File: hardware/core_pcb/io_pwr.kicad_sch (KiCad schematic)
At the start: 72 parts, among them J13 FIELD A 24V, J14 FIELD B 24V, J15 PUMP POWER, J16 PUMP SIGNALS, J17 RELAY COILS, J18 USB-C, Q1 2N7002, Q2 BC817, Q3 BC807, Q4 2N7002, Q5 BC817, Q6 BC807, U17 L78L05, U18 ISO7741, U19 74LVC1G08, U20 74LVC1G08, U21 IPS7091S, U22 74LVC1G14, U23 74LVC1G14, U24 LMV331, U25 CPC1017N, U26 CPC1017N, U27 USBLC6-2SC6

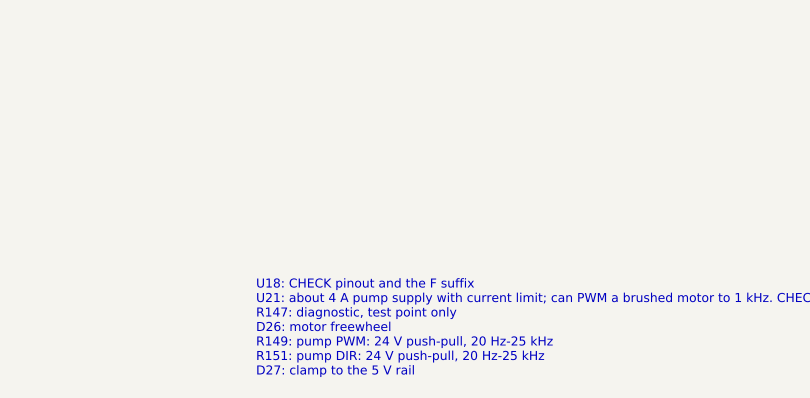
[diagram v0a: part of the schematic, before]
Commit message: CORE PCB: I/O chip pinouts checked against datasheets; gate latch, ODIS polarity
Pin tables of AD4112, ADS124S08, ISO2H823V2.5, ISO1I813T, ISO808A-1, ISO7741 and
ISOW7741 compared with the datasheets: all match. Fixes from the check: ISO2H823 /ODIS
is active low (takes GATE directly); OLADJ fitted 12.1k; CLKADJ 10k 0.1 %; ROSC 22.1k;
ISOW7741 EN/FLT pulled to 3.3 V; MAX6369 WDO only pulses, so a 74LVC1G175 latches a
trip until GATE_EN is re-armed. hardware/datasheets/IO_CHIPS_DATASHEET_CHECK.md holds the
extracts and the AD4112 register facts for the driver.

Co-Authored-By: Claude Opus 5.5 <noreply@anthropic.com>
Claude-Session: https://claude.ai/code/session_014onnq3eRiDkqdAB6fKiRDW
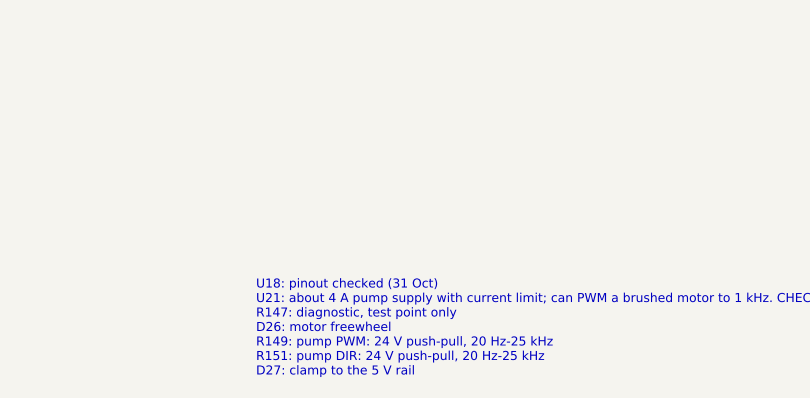
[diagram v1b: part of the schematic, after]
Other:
- note added: "U18: pinout checked (31 Oct) U21: about 4 A pump supply with current limit; can PWM a brushed motor to 1 kHz. CHECK rating once the 107Z current is known R147: diagnostic, test point only D26: motor freewheel R149: pump PWM: 24 V push-pull, 20 Hz-25 kHz R151: pump DIR: 24 V push-pull, 20 Hz-25 kHz D27: clamp to the 5 V rail"
- note removed: "U18: CHECK pinout and the F suffix U21: about 4 A pump supply with current limit; can PWM a brushed motor to 1 kHz. CHECK rating once the 107Z current is known R147: diagnostic, test point only D26: motor freewheel R149: pump PWM: 24 V push-pull, 20 Hz-25 kHz R151: pump DIR: 24 V push-pull, 20 Hz-25 kHz D27: clamp to the 5 V rail"
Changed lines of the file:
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@@
     (effects (font (size 1.0 1.0)) (justify left top))
   )
-  (text "\nU18: CHECK pinout and the F suffix\nU21: about 4 A pump supply with current limit; can PWM a brushed motor to 1 kHz. CHECK rating once the 107Z current is known\nR147: diagnostic, test point only\nD26: motor freewheel\nR149: pump PWM: 24 V push-pull, 20 Hz-25 kHz\nR151: pump DIR: 24 V push-pull, 20 Hz-25 kHz\nD27: clamp to the 5 V rail"
+  (text "\nU18: pinout checked (31 Oct)\nU21: about 4 A pump supply with current limit; can PWM a brushed motor to 1 kHz. CHECK rating once the 107Z current is known\nR147: diagnostic, test point only\nD26: motor freewheel\nR149: pump PWM: 24 V push-pull, 20 Hz-25 kHz\nR151: pump DIR: 24 V push-pull, 20 Hz-25 kHz\nD27: clamp to the 5 V rail"
     (at 203.2 347.98 0)
     (effects (font (size 1.0 1.0)) (justify left top))

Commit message: CORE PCB + breakout: make every user plug fit only its own header
Three pitch families (5.08 power/24 V outputs, 3.81 bank B, 3.5 sensors), one size per
header except the harmless temperature and 4-20 mA groups, and a coding key per header
(script-checked against every plug and shift). J13+J14 merged into one 4-way field plug;
pump power and signals on one 6-way plug (J16 gone); relays 3-way. Survival layer: 1k 1 W
pump outputs, per-channel relay PTCs + CPC1014N, 30 mA loop current limiters, TVS on the
5 V and 10 V sensor supplies. CORE_PCB.md section 15 has the mis-plug tables.

Co-Authored-By: Claude Opus 5.5 <noreply@anthropic.com>
Claude-Session: https://claude.ai/code/session_014onnq3eRiDkqdAB6fKiRDW
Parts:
- removed J14: FIELD B 24V, Connector_Phoenix_MSTB:PhoenixContact_MSTBVA_2,5_2-G-5,08_1x02_P5.08mm_Vertical, symbol Connector_Generic:Conn_01x02
- removed J16: PUMP SIGNALS, Connector_Phoenix_MC:PhoenixContact_MCV_1,5_4-G-3.81_1x04_P3.81mm_Vertical, symbol Connector_Generic:Conn_01x04
- added F22: 50mA, Fuse:Fuse_1206_3216Metric, symbol Device:Polyfuse
- F15: value 0.2A -> 50mA; MPN Bourns MF-NSMF020-2 -> Bourns MF-NSMF005-2
- J13: value FIELD A 24V -> FIELD 24V A+B; footprint Connector_Phoenix_MSTB:PhoenixContact_MSTBVA_2,5_2-G-5,08_1x02_P5.08mm_Vertical -> Connector_Phoenix_MSTB:PhoenixContact_MSTBVA_2,5_4-G-5,08_1x04_P5.08mm_Vertical; symbol Connector_Generic:Conn_01x02 -> Connector_Generic:Conn_01x04; MPN Phoenix MSTBVA 2,5/2-G-5,08 + plug (12 A) -> Phoenix MSTBVA 2,5/4-G-5,08 + coded, labelled plug; coding 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
- J15: value PUMP POWER -> PUMP; footprint Connector_Phoenix_MSTB:PhoenixContact_MSTBVA_2,5_2-G-5,08_1x02_P5.08mm_Vertical -> Connector_Phoenix_MSTB:PhoenixContact_MSTBVA_2,5_6-G-5,08_1x06_P5.08mm_Vertical; symbol Connector_Generic:Conn_01x02 -> Connector_Generic:Conn_01x06; MPN Phoenix MSTBVA 2,5/2-G-5,08 + plug -> Phoenix MSTBVA 2,5/6-G-5,08 + coded, labelled plug; coding 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
- J17: footprint Connector_Phoenix_MC:PhoenixContact_MCV_1,5_4-G-3.81_1x04_P3.81mm_Vertical -> Connector_Phoenix_MSTB:PhoenixContact_MSTBVA_2,5_3-G-5,08_1x03_P5.08mm_Vertical; symbol Connector_Generic:Conn_01x04 -> Connector_Generic:Conn_01x03; MPN Phoenix MCV 1,5/4-G-3,81 (or Degson / Dinkle equivalent) + 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 -> Phoenix MSTBVA 2,5/3-G-5,08 + coded, labelled plug; coding 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
- R149, R151: value 47R -> 1k 1W; footprint Resistor_SMD:R_0805_2012Metric -> Resistor_SMD:R_2512_6332Metric; MPN 47R -> anti-surge 2512, 1 W
- U25, U26: MPN IXYS CPC1017NTR -> IXYS CPC1014NTR
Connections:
- net +24V_FB: now also F22.1
- net FB_IN: now also J13.3 (Pin_3)
- net FIELD_0V: now also J13.4 (Pin_4), J15.6 (Pin_6), J17.3 (Pin_3); no longer J17.2 (Pin_2), J17.4 (Pin_4)
- net P_DIR_OUT: now also J15.4 (Pin_4)
- net P_PWM_OUT: now also J15.3 (Pin_3)
- net P_TACH_IN: now also J15.5 (Pin_5)
- net REL2_OUT: now also J17.2 (Pin_2); no longer J17.3 (Pin_3)
- net +24V_REL renamed +24V_REL1
- net +24V_REL1: no longer U26.3
- new net +24V_REL2: F22.2, U26.3
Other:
- note added: "Notes J13: one 4-way plug for both field supplies (12 A per contact): A = bank A, inputs, pump (about 10 A); B = bank B and relays (about 8 A). Link A and B in the plug for a single supply F12: bank A, inputs, ribbons F13: pump F14: bank B, relays D21: unidirectional TVS: surge clamp, and blows the fuse on reverse polarity U17: pump logic 5 V, field side U18: pinout checked (31 Oct)"
- note added: "U21: about 4 A pump supply with current limit; can PWM a brushed motor to 1 kHz. CHECK rating once the 107Z current is known R147: diagnostic, test point only D26: motor freewheel R149: pump PWM: 24 V push-pull, 20 Hz-25 kHz. 1k makes the output survive a short to 0 V or 24 V for ever (24 mA, 0.6 W). CHECK the 107Z input current (high level = 24 V - 1k x I) R151: pump DIR: 24 V push-pull, 20 Hz-2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"
- note added: "U24: CHECK pin order for the SOT-23-5 variant R156: hysteresis JP2: fit for an open-collector tacho J15: one plug for the whole pump: power, 0 V, PWM, DIR, tacho, signal 0 V (Thomas 107Z: signal ground must be field 0 V) F15: per-channel limit: a shorted coil wire trips only its own PTC U25: 60 V, 400 mA PhotoMOS: rides out a short until its PTC trips. CHECK with a 10 s short test R163: 5 V -> 3.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"
- note removed: "Notes J13: bank A, inputs, pump: about 10 A J14: bank B and relays: about 8 A F12: bank A, inputs, ribbons F13: pump F14: bank B, relays D21: unidirectional TVS: surge clamp, and blows the fuse on reverse polarity U17: pump logic 5 V, field side"
- note removed: "R154: 1.5 V threshold U24: CHECK pin order for the SOT-23-5 variant R156: hysteresis JP2: fit for an open-collector tacho J16: Thomas 107Z: signal ground must be field 0 V U25: 60 V, 100 mA PhotoMOS R163: 5 V -> 3.4 V"
- note removed: "U18: pinout checked (31 Oct) U21: about 4 A pump supply with current limit; can PWM a brushed motor to 1 kHz. CHECK rating once the 107Z current is known R147: diagnostic, test point only D26: motor freewheel R149: pump PWM: 24 V push-pull, 20 Hz-25 kHz R151: pump DIR: 24 V push-pull, 20 Hz-25 kHz D27: clamp to the 5 V rail"
- moved on the sheet: C125, C126, C127, C128, C129, C130, C131, C132, C133, C134, C135, C201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

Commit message: CORE PCB: fit-optional 4 x 4-20 mA analog outputs (AD5755-1, all DNP)
AD5755-1 on the analog island with its own ISOW7741 (CS_AO on PD3) and an ITX2405SA for
the boost converters; keyed 8-way 3.5 mm J26 (keys 2, 6, script-checked). Pin numbers from
the datasheet Table 5. Layout block plan now 2.8 mm over in io_pwr: the board is full
single-sided, see thread for the module option.

Co-Authored-By: Claude Opus 5.5 <noreply@anthropic.com>
Claude-Session: https://claude.ai/code/session_014onnq3eRiDkqdAB6fKiRDW
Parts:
- removed R143: 10k, Resistor_SMD:R_0805_2012Metric, symbol Device:R
- added R164: 68k, Resistor_SMD:R_0603_1608Metric, symbol Device:R
- R145: value 100k -> 10k; footprint Resistor_SMD:R_0603_1608Metric -> Resistor_SMD:R_0805_2012Metric; MPN 100k -> 10k
- R147: value 10k -> 100k; MPN 10k -> 100k
- R148: footprint Resistor_SMD:R_0805_2012Metric -> Resistor_SMD:R_0603_1608Metric
- R149, R151: value 1k 1W -> 10k; footprint Resistor_SMD:R_2512_6332Metric -> Resistor_SMD:R_0805_2012Metric; MPN anti-surge 2512, 1 W -> 10k
- R150, R152: value 10k -> 1k 1W; footprint Resistor_SMD:R_0805_2012Metric -> Resistor_SMD:R_2512_6332Metric; MPN 10k -> anti-surge 2512, 1 W
- R153: footprint Resistor_SMD:R_0603_1608Metric -> Resistor_SMD:R_0805_2012Metric
- R154: value 4k3 -> 10k; MPN 4k3 -> 10k
- R155: value 10k -> 4k3; MPN 10k -> 4k3
- R156: value 1M -> 10k; MPN 1M -> 10k
- R157: value 4k7 -> 1M; MPN 4k7 -> 1M
- R158: value 330R -> 4k7; MPN 330R -> 4k7
- R160: value 5k1 -> 330R; MPN 5k1 -> 330R
- R162: value 33k -> 5k1; MPN 33k -> 5k1
- R163: value 68k -> 33k; MPN 68k -> 33k
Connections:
- net +24V_FA: now also R144.1, R149.1, R151.1; no longer R148.1, R150.1
- net +24V_FB: now also R145.1; no longer R144.1
- net +5V_P: now also R148.1, R154.1, R156.1, R158.1; no longer R147.1, R153.1, R155.1, R157.1
- net FA_LED_A: now also R144.2
- net FB_LED_A: now also R145.2; no longer R144.2
- net FIELD_0V: now also R155.2; no longer R154.2
- net GATE: now also R160.1; no longer R158.1
- net GND: now also R147.2, R162.2, R164.2; no longer R145.2, R160.2, R163.2
- net PUMP_EN: now also R146.1; no longer R145.1
- net PUMP_PWM: now also R147.1; no longer R146.1
- net P_DG: now also R148.2; no longer R147.2
- net P_DIR_B: now also R151.2; no longer R150.2
- net P_DIR_E: now also R152.1; no longer R151.1
- net P_DIR_OUT: now also R152.2; no longer R151.2
- net P_PWM_B: now also R149.2; no longer R148.2
- net P_PWM_E: now also R150.1; no longer R149.1
- net P_PWM_OUT: now also R150.2; no longer R149.2
- net P_TACH_C: now also R153.2, R157.2; no longer R152.2, R156.2
- net P_TACH_F: now also R156.2, R157.1; no longer R155.2, R156.1
- net P_TACH_IN: now also R153.1; no longer R152.1
- net P_TACH_PU: now also R158.2; no longer R157.2
- net P_TREF: now also R154.2, R155.1; no longer R153.2, R154.1
- net REL1_A: now also R159.2; no longer R158.2
- net REL2_A: now also R160.2; no longer R159.2
- net USB_CC1: now also R161.1; no longer R160.1
- net USB_CC2: now also R162.1; no longer R161.1
- net USB_VBUS_SNS: now also R163.2, R164.1; no longer R162.2, R163.1
- net VBUS_USB: now also R163.1; no longer R162.1
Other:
- note added: "U21: about 4 A pump supply with current limit; can PWM a brushed motor to 1 kHz. CHECK rating once the 107Z current is known R148: diagnostic, test point only D26: motor freewheel R150: pump PWM: 24 V push-pull, 20 Hz-25 kHz. 1k makes the output survive a short to 0 V or 24 V for ever (24 mA, 0.6 W). CHECK the 107Z input current (high level = 24 V - 1k x I) R152: pump DIR: 24 V push-pull, 20 Hz-2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"
- note added: "U24: CHECK pin order for the SOT-23-5 variant R157: hysteresis JP2: fit for an open-collector tacho J15: one plug for the whole pump: power, 0 V, PWM, DIR, tacho, signal 0 V (Thomas 107Z: signal ground must be field 0 V) F15: per-channel limit: a shorted coil wire trips only its own PTC U25: 60 V, 400 mA PhotoMOS: rides out a short until its PTC trips. CHECK with a 10 s short test R164: 5 V -> 3.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"
- note removed: "U21: about 4 A pump supply with current limit; can PWM a brushed motor to 1 kHz. CHECK rating once the 107Z current is known R147: diagnostic, test point only D26: motor freewheel R149: pump PWM: 24 V push-pull, 20 Hz-25 kHz. 1k makes the output survive a short to 0 V or 24 V for ever (24 mA, 0.6 W). CHECK the 107Z input current (high level = 24 V - 1k x I) R151: pump DIR: 24 V push-pull, 20 Hz-2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"
- note removed: "U24: CHECK pin order for the SOT-23-5 variant R156: hysteresis JP2: fit for an open-collector tacho J15: one plug for the whole pump: power, 0 V, PWM, DIR, tacho, signal 0 V (Thomas 107Z: signal ground must be field 0 V) F15: per-channel limit: a shorted coil wire trips only its own PTC U25: 60 V, 400 mA PhotoMOS: rides out a short until its PTC trips. CHECK with a 10 s short test R163: 5 V -> 3.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"
- moved on the sheet: R144, R145, R146, R147, R148, R149, R150, R151, R152, R153, R154, R155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

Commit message: CORE PCB: SPI expansion header J26 for plug-on modules; analog outputs move off the core
Gary: analog out as an add-on module. J26 10-way latched IDC: +24 V and +3.3 V behind PTCs,
SPI4 through 100R, MISO buffered by a 74LVC1G125 enabled by CS_EXP (PD3), EXP_INT on PD7.
The AD5755-1 block drafted in 04adb9f is removed from the core and will become the module.
Layout block plan fits again. CORE_PCB.md section 16.

Co-Authored-By: Claude Opus 5.5 <noreply@anthropic.com>
Claude-Session: https://claude.ai/code/session_014onnq3eRiDkqdAB6fKiRDW
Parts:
- removed C125: 330n 50V, Capacitor_SMD:C_0603_1608Metric, symbol Device:C
- removed C126: 1u, Capacitor_SMD:C_0603_1608Metric, symbol Device:C
- removed R144, R145: 10k, Resistor_SMD:R_0805_2012Metric, symbol Device:R
- removed R146, R147: 100k, Resistor_SMD:R_0603_1608Metric, symbol Device:R
- removed R148: 10k, Resistor_SMD:R_0603_1608Metric, symbol Device:R
- added C136: 1n, Capacitor_SMD:C_0603_1608Metric, symbol Device:C
- added C137: 100n, Capacitor_SMD:C_0603_1608Metric, symbol Device:C
- added R165: 330R, Resistor_SMD:R_0603_1608Metric, symbol Device:R
- added R166, R167: 5k1, Resistor_SMD:R_0603_1608Metric, symbol Device:R
- added R168: 33k, Resistor_SMD:R_0603_1608Metric, symbol Device:R
- added R169: 68k, Resistor_SMD:R_0603_1608Metric, symbol Device:R
- C127: value 100n -> 330n 50V; MPN 100n -> 330n 50V
- C128: value 100n -> 1u; MPN 100n -> 1u
- C131: value 100n 50V -> 100n; MPN 100n 50V -> 100n
- C133: value 100n -> 100n 50V; MPN 100n -> 100n 50V
- C134: value 1n -> 100n; MPN 1n -> 100n
- R150: value 1k 1W -> 10k; footprint Resistor_SMD:R_2512_6332Metric -> Resistor_SMD:R_0805_2012Metric; MPN anti-surge 2512, 1 W -> 10k
- R151: value 10k -> 100k; footprint Resistor_SMD:R_0805_2012Metric -> Resistor_SMD:R_0603_1608Metric; MPN 10k -> 100k
- R152: value 1k 1W -> 100k; footprint Resistor_SMD:R_2512_6332Metric -> Resistor_SMD:R_0603_1608Metric; MPN anti-surge 2512, 1 W -> 100k
- R153: footprint Resistor_SMD:R_0805_2012Metric -> Resistor_SMD:R_0603_1608Metric
- R154, R156: footprint Resistor_SMD:R_0603_1608Metric -> Resistor_SMD:R_0805_2012Metric
- R155: value 4k3 -> 1k 1W; footprint Resistor_SMD:R_0603_1608Metric -> Resistor_SMD:R_2512_6332Metric; MPN 4k3 -> anti-surge 2512, 1 W
- R157: value 1M -> 1k 1W; footprint Resistor_SMD:R_0603_1608Metric -> Resistor_SMD:R_2512_6332Metric; MPN 1M -> anti-surge 2512, 1 W
- R158: value 4k7 -> 10k; footprint Resistor_SMD:R_0603_1608Metric -> Resistor_SMD:R_0805_2012Metric; MPN 4k7 -> 10k
- R159: value 330R -> 10k; MPN 330R -> 10k
- R160: value 330R -> 4k3; MPN 330R -> 4k3
- R161: value 5k1 -> 10k; MPN 5k1 -> 10k
- R162: value 5k1 -> 1M; MPN 5k1 -> 1M
- R163: value 33k -> 4k7; MPN 33k -> 4k7
- R164: value 68k -> 330R; MPN 68k -> 330R
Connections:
- net +24V_FA: now also C127.1, R154.1, R156.1; no longer R151.1
- net +24V_FB: now also R150.1
- net +24V_FP: now also C133.1; no longer C131.1
- net +3V3: now also C130.1, C131.1; no longer C127.1, C128.1
- net +5V_P: now also C128.1, C134.1, R153.1, R159.1, R161.1, R163.1, C137.1; no longer C130.1, C133.1, R154.1, R156.1, R158.1
- net FA_LED_A: now also R149.2
- net FB_LED_A: now also R150.2
- net FIELD_0V: now also C127.2, C128.2, R160.2, C136.2, C137.2; no longer C130.2, C131.2, R155.2
- net GATE: now also R164.1, R165.1; no longer R159.1, R160.1
- net GND: now also C130.2, C131.2, R151.2, R152.2, R166.2, R167.2, R169.2; no longer C127.2, C128.2, R161.2, R162.2, R164.2
- net PUMP_EN: now also R151.1
- net PUMP_PWM: now also R152.1
- net P_DG: now also R153.2
- net P_DIR_B: now also R156.2; no longer R151.2
- net P_DIR_E: now also R157.1; no longer R152.1
- net P_DIR_OUT: now also R157.2; no longer R152.2
- net P_PWM_B: now also R154.2; no longer R149.2
- net P_PWM_E: now also R155.1; no longer R150.1
- net P_PWM_OUT: now also R155.2; no longer R150.2
- net P_TACH_C: now also R158.2, R162.2, C136.1; no longer C134.1, R153.2, R157.2
- net P_TACH_F: now also R161.2, R162.1; no longer R156.2, R157.1
- net P_TACH_IN: now also R158.1; no longer R153.1
- net P_TACH_PU: now also R163.2; no longer R158.2
- net P_TREF: now also R159.2, R160.1; no longer R154.2, R155.1
- net REL1_A: now also R164.2; no longer R159.2
- net REL2_A: now also R165.2; no longer R160.2
- net USB_CC1: now also R166.1; no longer R161.1
- net USB_CC2: now also R167.1; no longer R162.1
- net USB_VBUS_SNS: now also R168.2, R169.1; no longer R163.2, R164.1
- net VBUS_USB: now also R168.1; no longer R163.1
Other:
- note added: "U21: about 4 A pump supply with current limit; can PWM a brushed motor to 1 kHz. CHECK rating once the 107Z current is known R153: diagnostic, test point only D26: motor freewheel R155: pump PWM: 24 V push-pull, 20 Hz-25 kHz. 1k makes the output survive a short to 0 V or 24 V for ever (24 mA, 0.6 W). CHECK the 107Z input current (high level = 24 V - 1k x I) R157: pump DIR: 24 V push-pull, 20 Hz-2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"
- note added: "U24: CHECK pin order for the SOT-23-5 variant R162: hysteresis JP2: fit for an open-collector tacho J15: one plug for the whole pump: power, 0 V, PWM, DIR, tacho, signal 0 V (Thomas 107Z: signal ground must be field 0 V) F15: per-channel limit: a shorted coil wire trips only its own PTC U25: 60 V, 400 mA PhotoMOS: rides out a short until its PTC trips. CHECK with a 10 s short test R169: 5 V -> 3.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"
- note removed: "U21: about 4 A pump supply with current limit; can PWM a brushed motor to 1 kHz. CHECK rating once the 107Z current is known R148: diagnostic, test point only D26: motor freewheel R150: pump PWM: 24 V push-pull, 20 Hz-25 kHz. 1k makes the output survive a short to 0 V or 24 V for ever (24 mA, 0.6 W). CHECK the 107Z input current (high level = 24 V - 1k x I) R152: pump DIR: 24 V push-pull, 20 Hz-2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"
- note removed: "U24: CHECK pin order for the SOT-23-5 variant R157: hysteresis JP2: fit for an open-collector tacho J15: one plug for the whole pump: power, 0 V, PWM, DIR, tacho, signal 0 V (Thomas 107Z: signal ground must be field 0 V) F15: per-channel limit: a shorted coil wire trips only its own PTC U25: 60 V, 400 mA PhotoMOS: rides out a short until its PTC trips. CHECK with a 10 s short test R164: 5 V -> 3.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"
- moved on the sheet: C127, C128, C129, C130, C131, C132, C133, C134, C135, R149, R150, R151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
